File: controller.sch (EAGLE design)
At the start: 28 parts, among them IC1 7805DT, J1 POWER_JACKSLT, J2 POWER_JACKSLT, Q1 MOSFET-NCHANNELBSS123LT1G, Q2 MOSFET-PCHANNEL, Q3 MOSFET-NCHANNELFDD8780, Q5 MMBT4403, U1 ATMEGA328P

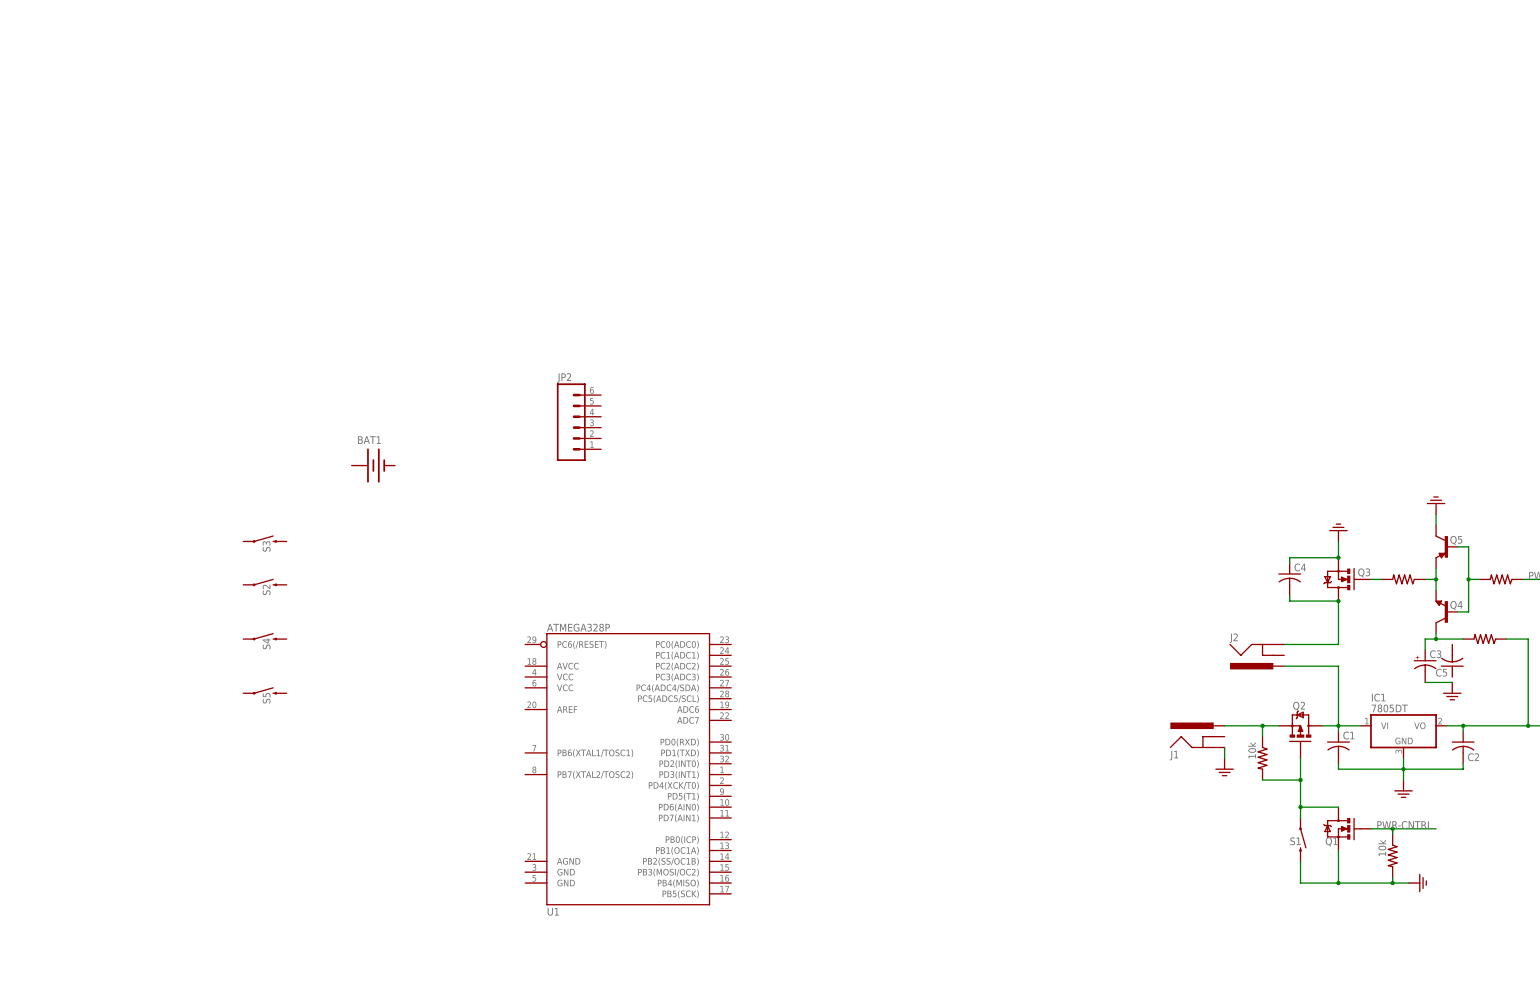
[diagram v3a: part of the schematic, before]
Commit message: began layout of mcu section
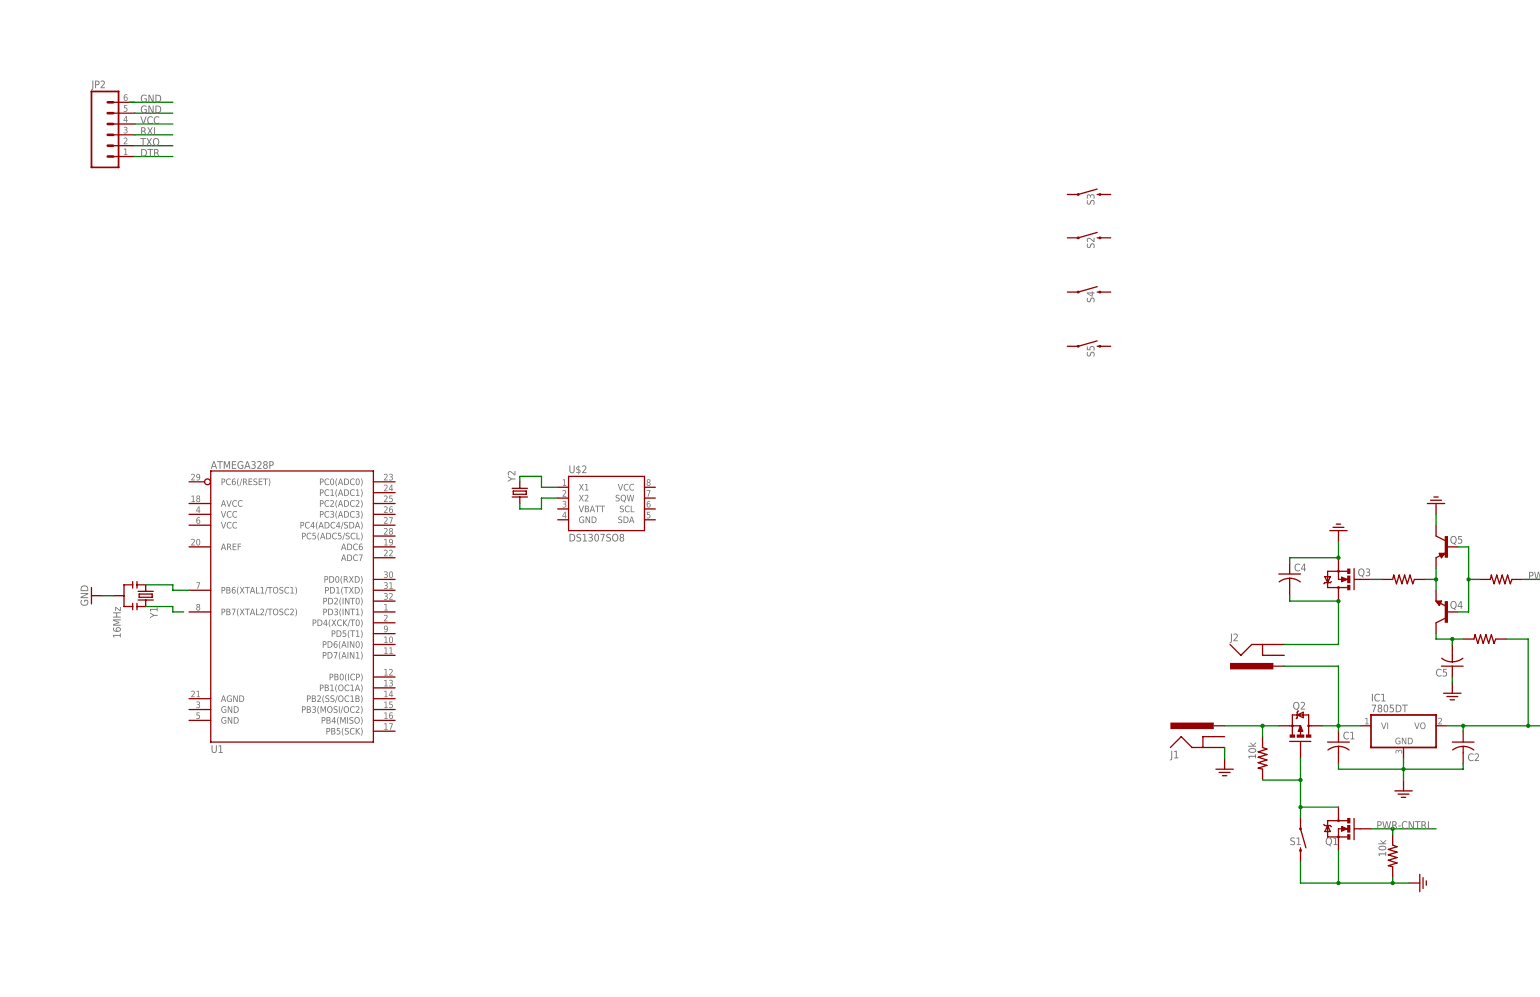
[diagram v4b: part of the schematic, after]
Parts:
- removed BAT1: (no value), SparkFun-Electromechanical:BATTERY12PTH
- removed C3: (no value), adafruit:CPOL-USE22-10AXIAL
- added U$2: DS1307SO8, SparkFun-FreqCtrl:DS1307SO8
- added Y1: 16MHz, SparkFun-FreqCtrl:RESONATOR16MHZ
- added Y2: (no value), SparkFun-FreqCtrl:CRYSTAL32-SMD
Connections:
- removed net 3.3V: C3.-
- new net DTR: JP2.1
- new net N$1: U1.PB6(XTAL1/TOSC1), Y1.1
- new net N$4: Y1.3
- new net N$6: U$2.X1, Y2.2
- new net N$7: U$2.X2, Y2.1
- new net RXI: JP2.3
- new net TXO: JP2.2
- new net VCC: JP2.4
- net GND: now also C5.1, JP2.5, Y1.2
- net N$2: now also C5.2; no longer C3.+
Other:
- moved on the sheet: JP2, S2, S3, S4, S5, U1
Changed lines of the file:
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@@
 <setting verticaltext="up"/>
 </settings>
-<grid distance="0.05" unitdist="inch" unit="inch" style="lines" multiple="1" display="no" altdistance="0.01" altunitdist="inch" altunit="inch"/>
+<grid distance="0.05" unitdist="inch" unit="inch" style="lines" multiple="1" display="yes" altdistance="0.01" altunitdist="inch" altunit="inch"/>
 <layers>
 <layer number="1" name="Top" color="4" fill="1" visible="no" active="no"/>
@@
 <part name="GND7" library="SparkFun-Aesthetics" deviceset="GND2" device=""/>
 <part name="U$7" library="jt_parts" deviceset="RESISTOR" device=""/>
-<part name="BAT1" library="SparkFun-Electromechanical" deviceset="BATTERY" device="12PTH"/>
 <part name="U1" library="SparkFun-DigitalIC" deviceset="ATMEGA328_SMT" device="" value="ATMEGA328P"/>
 <part name="S4" library="SparkFun-Electromechanical" deviceset="SWITCH-MOMENTARY-2" device="SIDE_EZ"/>
@@
 <part name="S2" library="SparkFun-Electromechanical" deviceset="SWITCH-MOMENTARY-2" device="SIDE_EZ"/>
 <part name="S3" library="SparkFun-Electromechanical" deviceset="SWITCH-MOMENTARY-2" device="SIDE_EZ"/>
-<part name="C3" library="adafruit" deviceset="CPOL-US" device="E22-10AXIAL"/>
+<part name="U$2" library="SparkFun-FreqCtrl" deviceset="DS1307" device="SO8"/>
+<part name="Y1" library="SparkFun-FreqCtrl" deviceset="RESONATOR" device="16MHZ" value="16MHz"/>
+<part name="GND" library="SparkFun-Aesthetics" deviceset="GND" device=""/>
+<part name="Y2" library="SparkFun-FreqCtrl" deviceset="CRYSTAL" device="32-SMD"/>
 </parts>
 <sheets>
@@
 <attribute name="VALUE" x="375.92" y="140.462" size="1.778" layer="96" rot="R180"/>
 </instance>
-<instance part="BAT1" gate="G$1" x="111.76" y="177.8"/>
-<instance part="U1" gate="G$1" x="170.18" y="110.49"/>
-<instance part="S4" gate="G$1" x="86.36" y="137.16" smashed="yes">
-<attribute name="NAME" x="87.63" y="134.62" size="1.778" layer="95" rot="R90"/>
-</instance>
-<instance part="S5" gate="G$1" x="86.36" y="124.46" smashed="yes">
-<attribute name="NAME" x="87.63" y="121.92" size="1.778" layer="95" rot="R90"/>
-</instance>
-<instance part="JP2" gate="G$1" x="160.02" y="186.69"/>
-<instance part="S2" gate="G$1" x="86.36" y="149.86" smashed="yes">
-<attribute name="NAME" x="87.63" y="147.32" size="1.778" layer="95" rot="R90"/>
-</instance>
-<instance part="S3" gate="G$1" x="86.36" y="160.02" smashed="yes">
-<attribute name="NAME" x="87.63" y="157.48" size="1.778" layer="95" rot="R90"/>
-</instance>
-<instance part="C3" gate="G$1" x="358.14" y="132.08"/>
+<instance part="U1" gate="G$1" x="91.44" y="148.59"/>
+<instance part="S4" gate="G$1" x="279.4" y="218.44" smashed="yes">
+<attribute name="NAME" x="280.67" y="215.9" size="1.778" layer="95" rot="R90"/>
+</instance>
+<instance part="S5" gate="G$1" x="279.4" y="205.74" smashed="yes">
+<attribute name="NAME" x="280.67" y="203.2" size="1.778" layer="95" rot="R90"/>
+</instance>
+<instance part="JP2" gate="G$1" x="50.8" y="255.27"/>
+<instance part="S2" gate="G$1" x="279.4" y="231.14" smashed="yes">
+<attribute name="NAME" x="280.67" y="228.6" size="1.778" layer="95" rot="R90"/>
+</instance>
+<instance part="S3" gate="G$1" x="279.4" y="241.3" smashed="yes">
+<attribute name="NAME" x="280.67" y="238.76" size="1.778" layer="95" rot="R90"/>
+</instance>
+<instance part="U$2" gate="G$1" x="165.1" y="170.18"/>
+<instance part="Y1" gate="G$1" x="58.42" y="147.32" rot="R270"/>
+<instance part="GND" gate="1" x="45.72" y="147.32" rot="R270"/>
+<instance part="Y2" gate="G$1" x="146.05" y="171.45" rot="R90"/>
 </instances>
 <busses>
@@
 <wire x1="360.68" y1="166.37" x2="360.68" y2="163.83" width="0.1524" layer="91"/>
 </segment>
+<segment>
+<pinref part="C5" gate="G$1" pin="1"/>
+<pinref part="GND7" gate="G$1" pin="3.3V"/>
+<wire x1="364.49" y1="128.27" x2="364.49" y2="127" width="0.1524" layer="91"/>
+</segment>
+<segment>
+<pinref part="Y1" gate="G$1" pin="2"/>
+<pinref part="GND" gate="1" pin="GND"/>
+<wire x1="50.8" y1="147.32" x2="48.26" y2="147.32" width="0.1524" layer="91"/>
+</segment>
+<segment>
+<wire x1="54.61" y1="262.89" x2="64.77" y2="262.89" width="0.1524" layer="91"/>
+<label x="57.15" y="262.89" size="1.778" layer="95"/>
+</segment>
+<segment>
+<pinref part="JP2" gate="G$1" pin="5"/>
+<wire x1="55.88" y1="260.35" x2="64.77" y2="260.35" width="0.1524" layer="91"/>
+<label x="57.15" y="260.35" size="1.778" layer="95"/>
+</segment>
 </net>
 <net name="RCK" class="0">
@@
 <pinref part="Q4" gate="G$1" pin="C"/>
 <wire x1="360.68" y1="138.43" x2="360.68" y2="137.16" width="0.1524" layer="91"/>
-<wire x1="360.68" y1="137.16" x2="367.03" y2="137.16" width="0.1524" layer="91"/>
+<wire x1="360.68" y1="137.16" x2="364.49" y2="137.16" width="0.1524" layer="91"/>
+<pinref part="C5" gate="G$1" pin="2"/>
+<wire x1="364.49" y1="137.16" x2="364.49" y2="135.89" width="0.1524" layer="91"/>
 <pinref part="U$7" gate="G$1" pin="2"/>
-<wire x1="360.68" y1="137.16" x2="358.14" y2="137.16" width="0.1524" layer="91"/>
-<junction x="360.68" y="137.16"/>
-<pinref part="C3" gate="G$1" pin="+"/>
-<wire x1="358.14" y1="134.62" x2="358.14" y2="137.16" width="0.1524" layer="91"/>
+<wire x1="364.49" y1="137.16" x2="367.03" y2="137.16" width="0.1524" layer="91"/>
+<junction x="364.49" y="137.16"/>
 </segment>
 </net>
@@
 </segment>
 </net>
-<net name="3.3V" class="0">
-<segment>
-<pinref part="GND7" gate="G$1" pin="3.3V"/>
-<pinref part="C3" gate="G$1" pin="-"/>
-<wire x1="364.49" y1="127" x2="358.14" y2="127" width="0.1524" layer="91"/>
-</segment>
-</net>
+<net name="N$1" class="0">
+<segment>
+<pinref part="U1" gate="G$1" pin="PB6(XTAL1/TOSC1)"/>
+<wire x1="68.58" y1="148.59" x2="64.77" y2="148.59" width="0.1524" layer="91"/>
+<wire x1="64.77" y1="148.59" x2="64.77" y2="149.86" width="0.1524" layer="91"/>
+<pinref part="Y1" gate="G$1" pin="1"/>
+<wire x1="64.77" y1="149.86" x2="58.42" y2="149.86" width="0.1524" layer="91"/>
+</segment>
+</net>
+<net name="N$4" class="0">
+<segment>
+<wire x1="67.31" y1="143.51" x2="64.77" y2="143.51" width="0.1524" layer="91"/>
+<wire x1="64.77" y1="143.51" x2="64.77" y2="144.78" width="0.1524" layer="91"/>
+<pinref part="Y1" gate="G$1" pin="3"/>
+<wire x1="64.77" y1="144.78" x2="58.42" y2="144.78" width="0.1524" layer="91"/>
+</segment>
+</net>
+<net name="VCC" class="0">
+<segment>
+<pinref part="JP2" gate="G$1" pin="4"/>
+<wire x1="55.88" y1="257.81" x2="64.77" y2="257.81" width="0.1524" layer="91"/>
+<label x="57.15" y="257.81" size="1.778" layer="95"/>
+</segment>
+</net>
+<net name="RXI" class="0">
+<segment>
+<pinref part="JP2" gate="G$1" pin="3"/>
+<wire x1="55.88" y1="255.27" x2="64.77" y2="255.27" width="0.1524" layer="91"/>
+<label x="57.15" y="255.27" size="1.778" layer="95"/>
+</segment>
+</net>
+<net name="TXO" class="0">
+<segment>
+<pinref part="JP2" gate="G$1" pin="2"/>
+<wire x1="55.88" y1="252.73" x2="64.77" y2="252.73" width="0.1524" layer="91"/>
+<label x="57.15" y="252.73" size="1.778" layer="95"/>
+</segment>
+</net>
+<net name="DTR" class="0">
+<segment>
+<pinref part="JP2" gate="G$1" pin="1"/>
+<wire x1="55.88" y1="250.19" x2="64.77" y2="250.19" width="0.1524" layer="91"/>
+<label x="57.15" y="250.19" size="1.778" layer="95"/>
+</segment>
+</net>
+<net name="N$6" class="0">
+<segment>
+<pinref part="U$2" gate="G$1" pin="X1"/>
+<wire x1="154.94" y1="172.72" x2="151.13" y2="172.72" width="0.1524" layer="91"/>
+<wire x1="151.13" y1="172.72" x2="151.13" y2="175.26" width="0.1524" layer="91"/>
+<wire x1="151.13" y1="175.26" x2="146.05" y2="175.26" width="0.1524" layer="91"/>
+<pinref part="Y2" gate="G$1" pin="2"/>
+<wire x1="146.05" y1="175.26" x2="146.05" y2="173.99" width="0.1524" layer="91"/>
+</segment>
+</net>
+<net name="N$7" class="0">
+<segment>
+<pinref part="U$2" gate="G$1" pin="X2"/>
+<wire x1="154.94" y1="170.18" x2="151.13" y2="170.18" width="0.1524" layer="91"/>
+<wire x1="151.13" y1="170.18" x2="151.13" y2="167.64" width="0.1524" layer="91"/>
+<wire x1="151.13" y1="167.64" x2="146.05" y2="167.64" width="0.1524" layer="91"/>
+<pinref part="Y2" gate="G$1" pin="1"/>
+<wire x1="146.05" y1="167.64" x2="146.05" y2="168.91" width="0.1524" layer="91"/>
+</segment>
+</net>

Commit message: completed micro section schematic. split power from led strip pwm sections.
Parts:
- removed J1, J2: POWER_JACKSLT, SparkFun-Connectors:POWER_JACKSLT
- removed Q1: MOSFET-NCHANNELBSS123LT1G, SparkFun-DiscreteSemi:MOSFET-NCHANNELBSS123LT1G
- removed Q2: MOSFET-PCHANNEL, SparkFun-DiscreteSemi:MOSFET-PCHANNEL
- added 12V_IN, LEDSTRIP: M02LOCK_LONGPADS, SparkFun-Connectors:M02LOCK_LONGPADS
- added C3: (no value), SparkFun-Capacitors:CAP_POL1206-KIT
- added C6, C7, C8: (no value), SparkFun-Capacitors:CAP0805
- added D1, D2, D3, D4, D5, D6: WHITE, SparkFun-LED:LED-WHITE
- added D7: GREEN, SparkFun-LED:LED-GREENLARGE
- added S6: (no value), SparkFun-Electromechanical:TAC_SWITCHSMD
- added U$8: (no value), jt_parts:RESISTOR
- C1: device adafruit:C-USC0805 -> SparkFun-Capacitors:CAP_POL1206-KIT
- C2, C4, C5: device adafruit:C-USC0805 -> SparkFun-Capacitors:CAP0805
- JP1: device SparkFun-Connectors:M06SIP -> SparkFun-Connectors:M06LOCK
- JP2: device SparkFun-Connectors:M06SIP -> SparkFun-Connectors:ARDUINO_SERIAL_PROGRAMLOCK
- S1: value SWITCH-MOMENTARY-2SIDE_EZ -> (none); device SparkFun-Electromechanical:SWITCH-MOMENTARY-2SIDE_EZ -> SparkFun-Electromechanical:SWITCH-SPDTPTH3
- U$3, U$4: value 10k -> (none)
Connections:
- removed net 12V-IN: J1.PWR, Q2.S, U$3.1
- removed net PWR-CNTRL: Q1.G, U$4.1
- new net N$11: C7.1, U1.AREF
- new net N$15: C8.2, S6.3, S6.4, U$8.2, U1.PC6(/RESET)
- new net N$8: 12V_IN.2, S1.P
- new net N$9: D1.A, D2.A, D3.A, D4.A, D5.A, D6.A, U$3.2
- new net NIGHT: U$3.1
- net 12V: now also C1.+, LEDSTRIP.1, S1.O, S1.S; no longer C1.1, J2.PWR, Q2.D
- net 12V-RETURN: now also LEDSTRIP.2; no longer J2.GND
- net 5V: now also C3.+, C6.1, U$4.2, U$8.1, U1.AVCC, U1.VCC@1, U1.VCC@2
- net DTR: now also C8.1, JP2.DTR; no longer JP2.1
- net GND: now also 12V_IN.1, C1.-, C3.-, C6.2, C7.2, D7.C, JP2.CTS, JP2.GND, S6.1, S6.2, U1.AGND, U1.GND@1, U1.GND@2; no longer C1.2, J1.GND, JP2.5, Q1.S, S1.2, U$4.2
- net N$10: now also D7.A, U$4.1; no longer Q1.D, Q2.G, S1.1, U$3.2
- net N$4: now also U1.PB7(XTAL2/TOSC2)
- net RXI: now also JP2.TXO; no longer JP2.3
- net TXO: now also JP2.RXI; no longer JP2.2
- net VCC: now also JP2.VCC; no longer JP2.4
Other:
- moved on the sheet: C2, C4, C5, JP1, JP2, Q3, Q4, Q5, U$2, Y1, Y2
